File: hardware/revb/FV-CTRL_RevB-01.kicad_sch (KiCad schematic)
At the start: 19 parts, among them J1 12V INPUT, J2 XL4015 A: 12/G/6/G, J3 XL4015 B: 12/G/6/G, J4 5V D24V25F5, Q1 IRF4905PBF, U3 LD1117V33

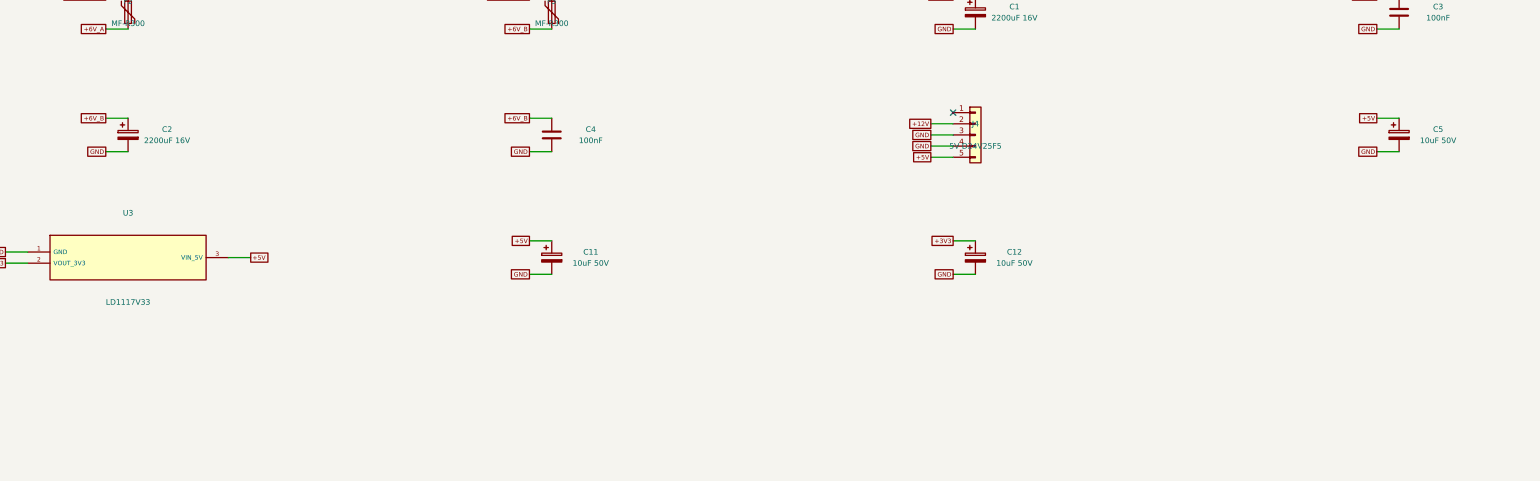
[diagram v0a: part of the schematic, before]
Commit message: fix(hardware): replace Pololu logic supply with RECOM 5V converter
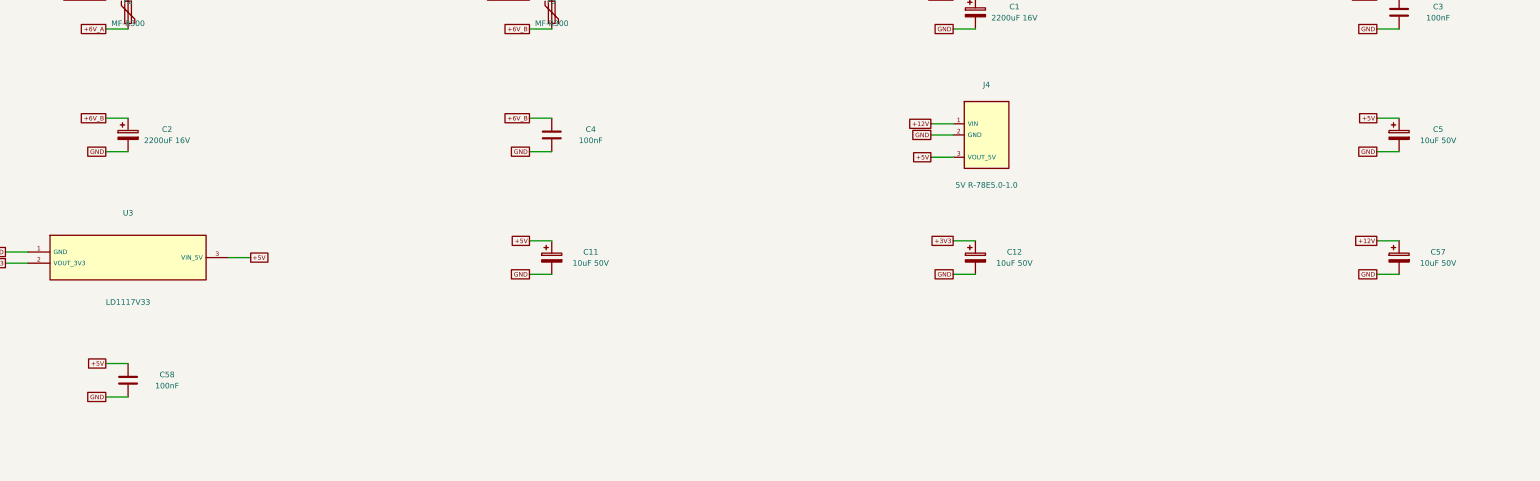
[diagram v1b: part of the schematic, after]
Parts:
- added C57: 10uF 50V, Capacitor_THT:CP_Radial_D5.0mm_P2.00mm, symbol Device:C_Polarized
- added C58: 100nF, Capacitor_SMD:C_0402_1005Metric, symbol Device:C
- J4: value 5V D24V25F5 -> 5V R-78E5.0-1.0; footprint fv_reva2:Pololu_D24V25F5 -> fv_modules:RECOM_R78E5V1A; symbol Connector_Generic:Conn_01x05 -> fv_revb:RECOM_R78E5V1A
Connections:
- net +12V: now also J4.1 (VIN), C57.1; no longer J4.2 (Pin_2)
- net +5V: now also J4.3 (VOUT_5V), C58.1; no longer J4.5 (Pin_5)
- net GND: now also J4.2 (GND), C57.2, C58.2; no longer J4.3 (Pin_3), J4.4 (Pin_4)
- no-connect marks 1 -> 0
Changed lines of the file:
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@@
 	)
 	(symbol
-		(lib_id "Connector_Generic:Conn_01x05")
+		(lib_id "fv_revb:RECOM_R78E5V1A")
 		(at 248.9200 124.4600 0)
 		(unit 1)
@@
 		(dnp no)
 		(property "Reference" "J4"
-			(at 248.9200 121.9200 0)
-			(effects (font (size 1.27 1.27)))
-		)
-		(property "Value" "5V D24V25F5"
-			(at 248.9200 127.0000 0)
-			(effects (font (size 1.27 1.27)))
-		)
-		(property "Footprint" "fv_reva2:Pololu_D24V25F5"
+			(at 251.4600 113.0300 0)
+			(effects (font (size 1.27 1.27)))
+		)
+		(property "Value" "5V R-78E5.0-1.0"
+			(at 251.4600 135.8900 0)
+			(effects (font (size 1.27 1.27)))
+		)
+		(property "Footprint" "fv_modules:RECOM_R78E5V1A"
 			(at 248.9200 124.4600 0)
 			(effects (font (size 1.27 1.27)) (hide yes))
@@
 		(pin "2")
 		(pin "3")
-		(pin "4")
-		(pin "5")
 	)
 	(symbol
@@
 		(pts
 			(xy 243.8400 124.4600) (xy 238.7600 124.4600)
-		)
-		(stroke (width 0) (type default))
-	)
-	(wire
-		(pts
-			(xy 243.8400 127.0000) (xy 238.7600 127.0000)
 		)
 		(stroke (width 0) (type default))
@@
 (global_label "+12V" (shape passive) (at 238.7600 121.9200 180) (effects (font (size 1.016 1.016)) (justify right)))
 (global_label "GND" (shape passive) (at 238.7600 124.4600 180) (effects (font (size 1.016 1.016)) (justify right)))
-(global_label "GND" (shape passive) (at 238.7600 127.0000 180) (effects (font (size 1.016 1.016)) (justify right)))
 (global_label "+5V" (shape passive) (at 238.7600 129.5400 180) (effects (font (size 1.016 1.016)) (justify right)))
 (global_label "+5V" (shape passive) (at 340.3600 120.6500 180) (effects (font (size 1.016 1.016)) (justify right)))
@@
 (global_label "+3V3" (shape passive) (at 243.8400 148.5900 180) (effects (font (size 1.016 1.016)) (justify right)))
 (global_label "GND" (shape passive) (at 243.8400 156.2100 180) (effects (font (size 1.016 1.016)) (justify right)))
-	(no_connect
-		(at 243.8400 119.3800)
-	)
 	(sheet_instances
 		(path "/"
@@
 		)
 	)
+	(symbol
+		(lib_id "Device:C_Polarized")
+		(at 345.4400 152.4000 0)
+		(unit 1)
+		(exclude_from_sim no)
+		(in_bom yes)
+		(on_board yes)
+		(dnp no)
+		(property "Reference" "C57"
+			(at 354.3300 151.1300 0)
+			(effects (font (size 1.27 1.27)))
+		)
+		(property "Value" "10uF 50V"
+			(at 354.3300 153.6700 0)
+			(effects (font (size 1.27 1.27)))
+		)
+		(property "Footprint" "Capacitor_THT:CP_Radial_D5.0mm_P2.00mm"
+			(at 345.4400 152.4000 0)
+			(effects (font (size 1.27 1.27)) (hide yes))
+		)
+		(property "Datasheet" "~"
+			(at 345.4400 152.4000 0)
+			(effects (font (size 1.27 1.27)) (hide yes))
+		)
+		(property "Description" ""
+			(at 345.4400 152.4000 0)
+			(effects (font (size 1.27 1.27)) (hide yes))
+		)
+		(pin "1")
+		(pin "2")
+	)
+	(wire
+		(pts
+			(xy 345.4400 148.5900) (xy 340.3600 148.5900)
+		)
+		(stroke (width 0) (type default))
+	)
+	(wire
+		(pts
+			(xy 345.4400 156.2100) (xy 340.3600 156.2100)
+		)
+		(stroke (width 0) (type default))
+	)
+	(global_label "+12V" (shape passive) (at 340.3600 148.5900 180) (effects (font (size 1.016 1.016)) (justify right)))
+	(global_label "GND" (shape passive) (at 340.3600 156.2100 180) (effects (font (size 1.016 1.016)) (justify right)))
+	(symbol
+		(lib_id "Device:C")
+		(at 55.8800 180.3400 0)
+		(unit 1)
+		(exclude_from_sim no)
+		(in_bom yes)
+		(on_board yes)
+		(dnp no)
+		(property "Reference" "C58"
+			(at 64.7700 179.0700 0)
+			(effects (font (size 1.27 1.27)))
+		)
+		(property "Value" "100nF"
+			(at 64.7700 181.6100 0)
+			(effects (font (size 1.27 1.27)))
+		)
+		(property "Footprint" "Capacitor_SMD:C_0402_1005Metric"
+			(at 55.8800 180.3400 0)
+			(effects (font (size 1.27 1.27)) (hide yes))
+		)
+		(property "Datasheet" "~"
+			(at 55.8800 180.3400 0)
+			(effects (font (size 1.27 1.27)) (hide yes))
+		)
+		(property "Description" ""
+			(at 55.8800 180.3400 0)
+			(effects (font (size 1.27 1.27)) (hide yes))
+		)
+		(pin "1")
+		(pin "2")
+	)
+	(wire
+		(pts
+			(xy 55.8800 176.5300) (xy 50.8000 176.5300)
+		)
+		(stroke (width 0) (type default))
+	)
+	(wire
+		(pts
+			(xy 55.8800 184.1500) (xy 50.8000 184.1500)
+		)
+		(stroke (width 0) (type default))
+	)
+	(global_label "+5V" (shape passive) (at 50.8000 176.5300 180) (effects (font (size 1.016 1.016)) (justify right)))
+	(global_label "GND" (shape passive) (at 50.8000 184.1500 180) (effects (font (size 1.016 1.016)) (justify right)))
 )

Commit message: feat(hardware): upgrade RevB passives to 0603 footprints and enhance DFM routing
- Convert all sub-0603 passives to 0603 footprints across schematics and PCB
- Enforce minimum track width >= 0.15mm and add safe GND stitching vias
- Verify clean schematic parity, 0 ERC errors, 0 electrical DRC errors, and via-paste clearance
- Add dedicated routing and QFN escape tools
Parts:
- C58: footprint Capacitor_SMD:C_0402_1005Metric -> Capacitor_SMD:C_0603_1608Metric
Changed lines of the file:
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@@
 			(effects (font (size 1.27 1.27)))
 		)
-		(property "Footprint" "Capacitor_SMD:C_0402_1005Metric"
+		(property "Footprint" "Capacitor_SMD:C_0603_1608Metric"
 			(at 55.8800 180.3400 0)
 			(effects (font (size 1.27 1.27)) (hide yes))
